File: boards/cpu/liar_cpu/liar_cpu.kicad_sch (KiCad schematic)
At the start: 18 parts, among them J1 Conn_01x06, J2 Conn_02x10_Top_Bottom, J3 Conn_01x06, SW1 SW_DIP_x04, U1 74HC161, U2 27C512, U3 74HC283, U4 74HC161, U5 74HC161

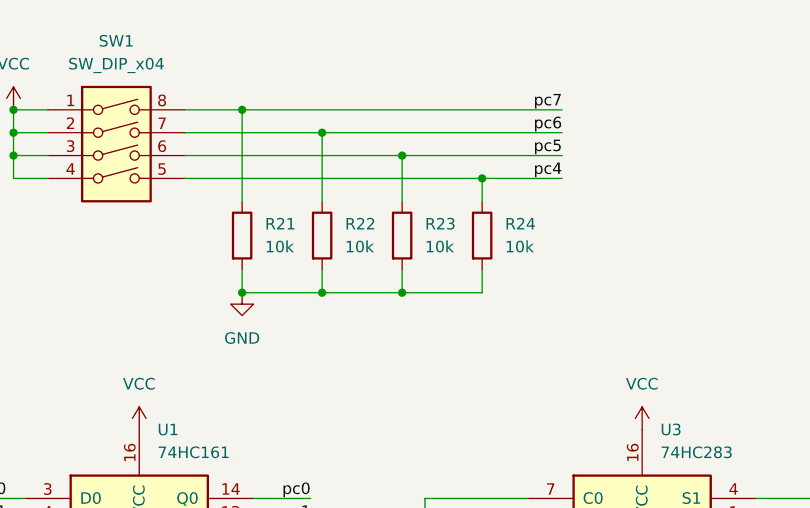
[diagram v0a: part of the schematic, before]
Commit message: liar_cpu: add board design
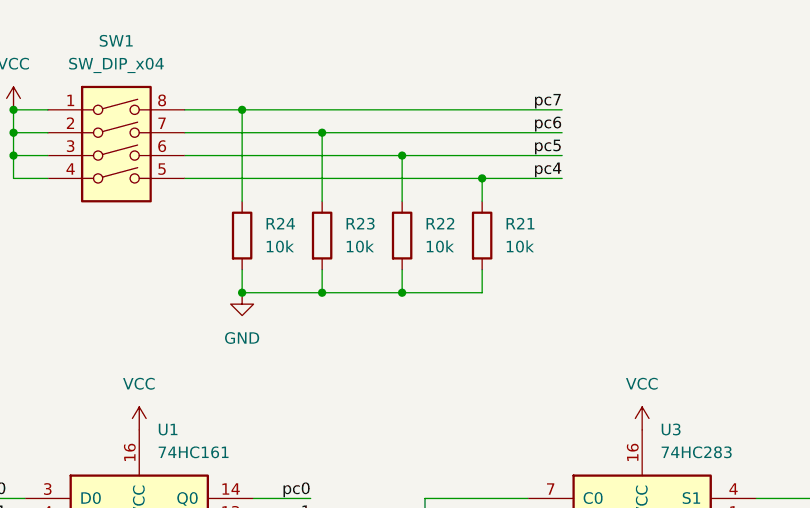
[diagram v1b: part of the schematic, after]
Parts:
- renumbered R24 to R21, R23 to R22, R22 to R23, R21 to R24
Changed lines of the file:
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@@
   (symbol (lib_id "Device:R") (at 123.19 38.1 0) (unit 1)
     (in_bom yes) (on_board yes)
-    (property "Reference" "R22" (id 0) (at 125.73 36.8299 0)
+    (property "Reference" "R23" (id 0) (at 125.73 36.8299 0)
       (effects (font (size 1.27 1.27)) (justify left))
     )
@@
   (symbol (lib_id "Device:R") (at 140.97 38.1 0) (unit 1)
     (in_bom yes) (on_board yes) (fields_autoplaced)
-    (property "Reference" "R24" (id 0) (at 143.51 36.8299 0)
+    (property "Reference" "R21" (id 0) (at 143.51 36.8299 0)
       (effects (font (size 1.27 1.27)) (justify left))
     )
@@
   (symbol (lib_id "Device:R") (at 132.08 38.1 0) (unit 1)
     (in_bom yes) (on_board yes) (fields_autoplaced)
-    (property "Reference" "R23" (id 0) (at 134.62 36.8299 0)
+    (property "Reference" "R22" (id 0) (at 134.62 36.8299 0)
       (effects (font (size 1.27 1.27)) (justify left))
     )
@@
   (symbol (lib_id "Device:R") (at 114.3 38.1 0) (unit 1)
     (in_bom yes) (on_board yes) (fields_autoplaced)
-    (property "Reference" "R21" (id 0) (at 116.84 36.8299 0)
+    (property "Reference" "R24" (id 0) (at 116.84 36.8299 0)
       (effects (font (size 1.27 1.27)) (justify left))
     )
@@
       (reference "R20") (unit 1) (value "3.9k") (footprint "Resistor_SMD:R_0805_2012Metric_Pad1.20x1.40mm_HandSolder")
     )
+    (path "/629fdb7a-7978-43d0-987e-b84465775826"
+      (reference "R21") (unit 1) (value "10k") (footprint "Resistor_SMD:R_0805_2012Metric_Pad1.20x1.40mm_HandSolder")
+    )
+    (path "/8ef1307e-4e79-474d-a93c-be38f714571c"
+      (reference "R22") (unit 1) (value "10k") (footprint "Resistor_SMD:R_0805_2012Metric_Pad1.20x1.40mm_HandSolder")
+    )
+    (path "/2e36ce87-4661-4b8f-956a-16dc559e1b50"
+      (reference "R23") (unit 1) (value "10k") (footprint "Resistor_SMD:R_0805_2012Metric_Pad1.20x1.40mm_HandSolder")
+    )
     (path "/e77c17df-b20e-4e7d-b937-f281c75a0014"
-      (reference "R21") (unit 1) (value "10k") (footprint "Resistor_SMD:R_0805_2012Metric_Pad1.20x1.40mm_HandSolder")
-    )
-    (path "/2e36ce87-4661-4b8f-956a-16dc559e1b50"
-      (reference "R22") (unit 1) (value "10k") (footprint "Resistor_SMD:R_0805_2012Metric_Pad1.20x1.40mm_HandSolder")
-    )
-    (path "/8ef1307e-4e79-474d-a93c-be38f714571c"
-      (reference "R23") (unit 1) (value "10k") (footprint "Resistor_SMD:R_0805_2012Metric_Pad1.20x1.40mm_HandSolder")
-    )
-    (path "/629fdb7a-7978-43d0-987e-b84465775826"
       (reference "R24") (unit 1) (value "10k") (footprint "Resistor_SMD:R_0805_2012Metric_Pad1.20x1.40mm_HandSolder")
     )
